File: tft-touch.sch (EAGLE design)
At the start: 2 parts

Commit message: As ordered
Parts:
- added CONN1: STEMMA_I2C_QT, 00jim:STEMMA_I2C_QT
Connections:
- new net SCL: CONN1G$1.SCL, JP1.IO22_SCL
- new net SDA: CONN1G$1.SDA, JP1.IO21_SDA
- net GND: now also CONN1G$1.GND
- net S_CS: now also JP1.IO00_XX; no longer JP1.IO22_SCL
- net T_CS: now also JP1.VP; no longer JP1.IO21_SDA
- net VCC: now also CONN1G$1.V+
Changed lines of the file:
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@@
 <part name="U$1" library="00jim" deviceset="SPI_TFT_TOUCH" device=""/>
 <part name="JP1" library="00jim" deviceset="TTGO-TS-ESP32" device=""/>
+<part name="CONN1" library="00jim" deviceset="STEMMA_I2C" device="_QT"/>
 </parts>
 <sheets>
@@
 <attribute name="NAME" x="52.07" y="76.835" size="1.778" layer="95"/>
 <attribute name="VALUE" x="52.07" y="20.32" size="1.778" layer="96"/>
+</instance>
+<instance part="CONN1" gate="G$1" x="116.84" y="66.04" smashed="yes">
+<attribute name="NAME" x="113.03" y="74.295" size="1.778" layer="95"/>
+<attribute name="VALUE" x="113.03" y="58.42" size="1.778" layer="96"/>
 </instance>
 </instances>
@@
 <label x="83.82" y="43.18" size="1.778" layer="95"/>
 </segment>
+<segment>
+<pinref part="CONN1" gate="G$1" pin="GND"/>
+<wire x1="116.84" y1="71.12" x2="106.68" y2="71.12" width="0.1524" layer="91"/>
+<label x="106.68" y="71.12" size="1.778" layer="95"/>
+</segment>
 </net>
 <net name="VCC" class="0">
@@
 <wire x1="93.98" y1="58.42" x2="83.82" y2="58.42" width="0.1524" layer="91"/>
 <label x="83.82" y="58.42" size="1.778" layer="95"/>
+</segment>
+<segment>
+<pinref part="CONN1" gate="G$1" pin="V+"/>
+<wire x1="116.84" y1="68.58" x2="106.68" y2="68.58" width="0.1524" layer="91"/>
+<label x="106.68" y="68.58" size="1.778" layer="95"/>
 </segment>
 </net>
@@
 </segment>
 <segment>
-<pinref part="JP1" gate="G$1" pin="IO21_SDA"/>
-<wire x1="55.88" y1="40.64" x2="45.72" y2="40.64" width="0.1524" layer="91"/>
-<label x="45.72" y="40.64" size="1.778" layer="95"/>
+<pinref part="JP1" gate="G$1" pin="VP"/>
+<wire x1="55.88" y1="71.12" x2="45.72" y2="71.12" width="0.1524" layer="91"/>
+<label x="45.72" y="71.12" size="1.778" layer="95"/>
 </segment>
 </net>
@@
 </segment>
 <segment>
-<pinref part="JP1" gate="G$1" pin="IO22_SCL"/>
-<wire x1="55.88" y1="35.56" x2="45.72" y2="35.56" width="0.1524" layer="91"/>
-<label x="45.72" y="35.56" size="1.778" layer="95"/>
+<pinref part="JP1" gate="G$1" pin="IO00_XX"/>
+<wire x1="55.88" y1="53.34" x2="45.72" y2="53.34" width="0.1524" layer="91"/>
+<label x="45.72" y="53.34" size="1.778" layer="95"/>
 </segment>
 </net>
@@
 </segment>
 </net>
+<net name="SDA" class="0">
+<segment>
+<pinref part="JP1" gate="G$1" pin="IO21_SDA"/>
+<wire x1="55.88" y1="40.64" x2="45.72" y2="40.64" width="0.1524" layer="91"/>
+<label x="45.72" y="40.64" size="1.778" layer="95"/>
+</segment>
+<segment>
+<pinref part="CONN1" gate="G$1" pin="SDA"/>
+<wire x1="116.84" y1="66.04" x2="106.68" y2="66.04" width="0.1524" layer="91"/>
+<label x="106.68" y="66.04" size="1.778" layer="95"/>
+</segment>
+</net>
+<net name="SCL" class="0">
+<segment>
+<pinref part="JP1" gate="G$1" pin="IO22_SCL"/>
+<wire x1="55.88" y1="35.56" x2="45.72" y2="35.56" width="0.1524" layer="91"/>
+<label x="45.72" y="35.56" size="1.778" layer="95"/>
+</segment>
+<segment>
+<pinref part="CONN1" gate="G$1" pin="SCL"/>
+<wire x1="116.84" y1="63.5" x2="106.68" y2="63.5" width="0.1524" layer="91"/>
+<label x="106.68" y="63.5" size="1.778" layer="95"/>
+</segment>
+</net>

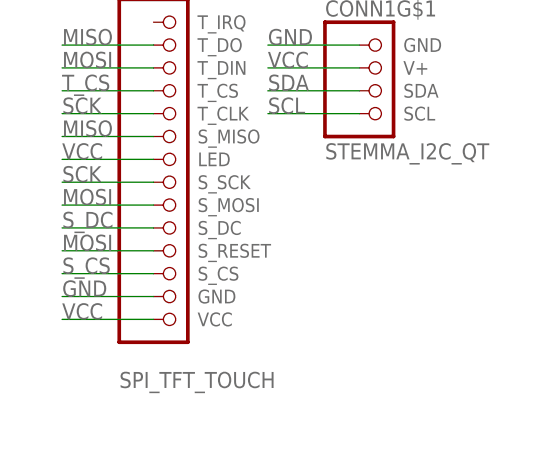
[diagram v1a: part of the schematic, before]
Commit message: Added more trinkets to TFT touch boards
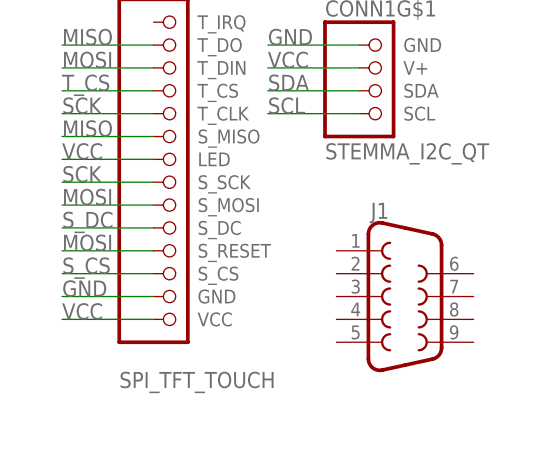
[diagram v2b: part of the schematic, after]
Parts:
- added J1: (no value), SparkFun-Connectors:DB9FEMALE
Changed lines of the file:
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@@
 <grid distance="0.1" unitdist="inch" unit="inch" style="lines" multiple="1" display="no" altdistance="0.01" altunitdist="inch" altunit="inch"/>
 <layers>
-<layer number="1" name="Top" color="4" fill="1" visible="no" active="no"/>
-<layer number="16" name="Bottom" color="1" fill="1" visible="no" active="no"/>
-<layer number="17" name="Pads" color="2" fill="1" visible="no" active="no"/>
-<layer number="18" name="Vias" color="2" fill="1" visible="no" active="no"/>
-<layer number="19" name="Unrouted" color="6" fill="1" visible="no" active="no"/>
-<layer number="20" name="Dimension" color="24" fill="1" visible="no" active="no"/>
-<layer number="21" name="tPlace" color="7" fill="1" visible="no" active="no"/>
-<layer number="22" name="bPlace" color="7" fill="1" visible="no" active="no"/>
-<layer number="23" name="tOrigins" color="15" fill="1" visible="no" active="no"/>
-<layer number="24" name="bOrigins" color="15" fill="1" visible="no" active="no"/>
-<layer number="25" name="tNames" color="7" fill="1" visible="no" active="no"/>
-<layer number="26" name="bNames" color="7" fill="1" visible="no" active="no"/>
-<layer number="27" name="tValues" color="7" fill="1" visible="no" active="no"/>
-<layer number="28" name="bValues" color="7" fill="1" visible="no" active="no"/>
+<layer number="1" name="Top" color="4" fill="1" visible="yes" active="no"/>
+<layer number="16" name="Bottom" color="1" fill="1" visible="yes" active="no"/>
+<layer number="17" name="Pads" color="2" fill="1" visible="yes" active="no"/>
+<layer number="18" name="Vias" color="2" fill="1" visible="yes" active="no"/>
+<layer number="19" name="Unrouted" color="6" fill="1" visible="yes" active="no"/>
+<layer number="20" name="Dimension" color="24" fill="1" visible="yes" active="no"/>
+<layer number="21" name="tPlace" color="7" fill="1" visible="yes" active="no"/>
+<layer number="22" name="bPlace" color="7" fill="1" visible="yes" active="no"/>
+<layer number="23" name="tOrigins" color="15" fill="1" visible="yes" active="no"/>
+<layer number="24" name="bOrigins" color="15" fill="1" visible="yes" active="no"/>
+<layer number="25" name="tNames" color="7" fill="1" visible="yes" active="no"/>
+<layer number="26" name="bNames" color="7" fill="1" visible="yes" active="no"/>
+<layer number="27" name="tValues" color="7" fill="1" visible="yes" active="no"/>
+<layer number="28" name="bValues" color="7" fill="1" visible="yes" active="no"/>
 <layer number="29" name="tStop" color="7" fill="3" visible="no" active="no"/>
 <layer number="30" name="bStop" color="7" fill="6" visible="no" active="no"/>
@@
 <layer number="35" name="tGlue" color="7" fill="4" visible="no" active="no"/>
 <layer number="36" name="bGlue" color="7" fill="5" visible="no" active="no"/>
-<layer number="37" name="tTest" color="7" fill="1" visible="no" active="no"/>
-<layer number="38" name="bTest" color="7" fill="1" visible="no" active="no"/>
+<layer number="37" name="tTest" color="7" fill="1" visible="yes" active="no"/>
+<layer number="38" name="bTest" color="7" fill="1" visible="yes" active="no"/>
 <layer number="39" name="tKeepout" color="4" fill="11" visible="no" active="no"/>
 <layer number="40" name="bKeepout" color="1" fill="11" visible="no" active="no"/>
@@
 <layer number="44" name="Drills" color="7" fill="1" visible="no" active="no"/>
 <layer number="45" name="Holes" color="7" fill="1" visible="no" active="no"/>
-<layer number="46" name="Milling" color="3" fill="1" visible="no" active="no"/>
-<layer number="47" name="Measures" color="7" fill="1" visible="no" active="no"/>
-<layer number="48" name="Document" color="7" fill="1" visible="no" active="no"/>
-<layer number="49" name="Reference" color="7" fill="1" visible="no" active="no"/>
-<layer number="50" name="dxf" color="7" fill="1" visible="no" active="no"/>
-<layer number="51" name="tDocu" color="7" fill="1" visible="no" active="no"/>
-<layer number="52" name="bDocu" color="7" fill="1" visible="no" active="no"/>
-<layer number="53" name="tGND_GNDA" color="7" fill="9" visible="no" active="no"/>
-<layer number="54" name="bGND_GNDA" color="1" fill="9" visible="no" active="no"/>
-<layer number="56" name="wert" color="7" fill="1" visible="no" active="no"/>
-<layer number="57" name="tCAD" color="7" fill="1" visible="no" active="no"/>
-<layer number="58" name="b3D" color="7" fill="1" visible="no" active="no"/>
-<layer number="59" name="tCarbon" color="7" fill="1" visible="no" active="no"/>
-<layer number="60" name="bCarbon" color="7" fill="1" visible="no" active="no"/>
-<layer number="61" name="stand" color="7" fill="1" visible="no" active="no"/>
+<layer number="46" name="Milling" color="3" fill="1" visible="yes" active="no"/>
+<layer number="47" name="Measures" color="7" fill="1" visible="yes" active="no"/>
+<layer number="48" name="Document" color="7" fill="1" visible="yes" active="no"/>
+<layer number="49" name="Reference" color="7" fill="1" visible="yes" active="no"/>
+<layer number="50" name="dxf" color="7" fill="1" visible="yes" active="no"/>
+<layer number="51" name="tDocu" color="7" fill="1" visible="yes" active="no"/>
+<layer number="52" name="bDocu" color="7" fill="1" visible="yes" active="no"/>
+<layer number="53" name="tGND_GNDA" color="7" fill="9" visible="yes" active="no"/>
+<layer number="54" name="bGND_GNDA" color="1" fill="9" visible="yes" active="no"/>
+<layer number="56" name="wert" color="7" fill="1" visible="yes" active="no"/>
+<layer number="57" name="tCAD" color="7" fill="1" visible="yes" active="no"/>
+<layer number="58" name="b3D" color="7" fill="1" visible="yes" active="no"/>
+<layer number="59" name="tCarbon" color="7" fill="1" visible="yes" active="no"/>
+<layer number="60" name="bCarbon" color="7" fill="1" visible="yes" active="no"/>
+<layer number="61" name="stand" color="7" fill="1" visible="yes" active="no"/>
 <layer number="88" name="SimResults" color="9" fill="1" visible="yes" active="yes"/>
 <layer number="89" name="SimProbes" color="9" fill="1" visible="yes" active="yes"/>
@@
 <part name="JP1" library="00jim" deviceset="TTGO-TS-ESP32" device=""/>
 <part name="CONN1" library="00jim" deviceset="STEMMA_I2C" device="_QT"/>
+<part name="J1" library="SparkFun-Connectors" deviceset="DB9" device="FEMALE"/>
 </parts>
 <sheets>
@@
 <attribute name="VALUE" x="113.03" y="58.42" size="1.778" layer="96"/>
 </instance>
+<instance part="J1" gate="G$1" x="121.92" y="43.18" smashed="yes">
+<attribute name="VALUE" x="118.11" y="34.798" size="1.778" layer="96" font="vector" align="top-left"/>
+<attribute name="NAME" x="118.11" y="51.816" size="1.778" layer="95" font="vector"/>
+</instance>
 </instances>

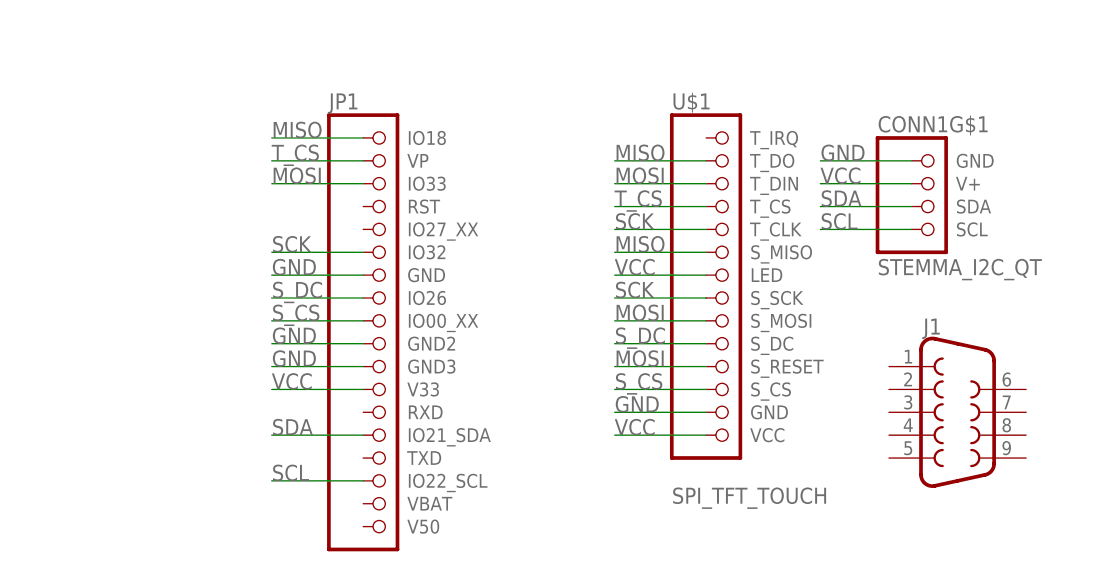
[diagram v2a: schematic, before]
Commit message: Fix board bug, order again
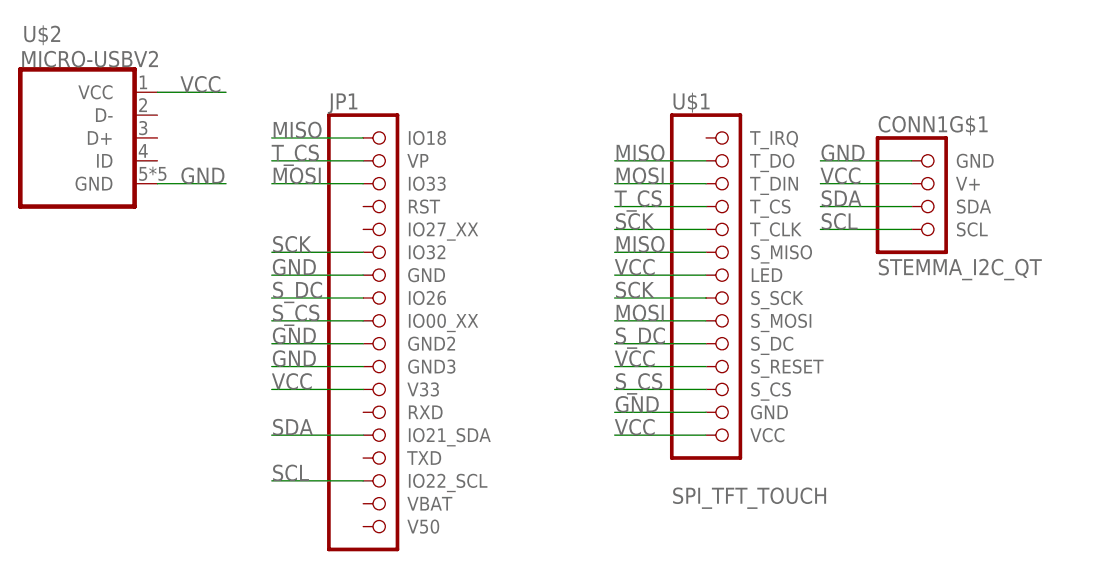
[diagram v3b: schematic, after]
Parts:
- removed J1: (no value), SparkFun-Connectors:DB9FEMALE
- added U$2: MICRO-USBV2, microusb:MICRO-USBV2
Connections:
- net GND: now also U$2.GND
- net MOSI: no longer U$1.S_RESET
- net VCC: now also U$1.S_RESET, U$2.VCC
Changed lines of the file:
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@@
 <grid distance="0.1" unitdist="inch" unit="inch" style="lines" multiple="1" display="no" altdistance="0.01" altunitdist="inch" altunit="inch"/>
 <layers>
-<layer number="1" name="Top" color="4" fill="1" visible="yes" active="no"/>
-<layer number="16" name="Bottom" color="1" fill="1" visible="yes" active="no"/>
-<layer number="17" name="Pads" color="2" fill="1" visible="yes" active="no"/>
-<layer number="18" name="Vias" color="2" fill="1" visible="yes" active="no"/>
-<layer number="19" name="Unrouted" color="6" fill="1" visible="yes" active="no"/>
-<layer number="20" name="Dimension" color="24" fill="1" visible="yes" active="no"/>
-<layer number="21" name="tPlace" color="7" fill="1" visible="yes" active="no"/>
-<layer number="22" name="bPlace" color="7" fill="1" visible="yes" active="no"/>
-<layer number="23" name="tOrigins" color="15" fill="1" visible="yes" active="no"/>
-<layer number="24" name="bOrigins" color="15" fill="1" visible="yes" active="no"/>
-<layer number="25" name="tNames" color="7" fill="1" visible="yes" active="no"/>
-<layer number="26" name="bNames" color="7" fill="1" visible="yes" active="no"/>
-<layer number="27" name="tValues" color="7" fill="1" visible="yes" active="no"/>
-<layer number="28" name="bValues" color="7" fill="1" visible="yes" active="no"/>
+<layer number="1" name="Top" color="4" fill="1" visible="no" active="no"/>
+<layer number="16" name="Bottom" color="1" fill="1" visible="no" active="no"/>
+<layer number="17" name="Pads" color="2" fill="1" visible="no" active="no"/>
+<layer number="18" name="Vias" color="2" fill="1" visible="no" active="no"/>
+<layer number="19" name="Unrouted" color="6" fill="1" visible="no" active="no"/>
+<layer number="20" name="Dimension" color="24" fill="1" visible="no" active="no"/>
+<layer number="21" name="tPlace" color="7" fill="1" visible="no" active="no"/>
+<layer number="22" name="bPlace" color="7" fill="1" visible="no" active="no"/>
+<layer number="23" name="tOrigins" color="15" fill="1" visible="no" active="no"/>
+<layer number="24" name="bOrigins" color="15" fill="1" visible="no" active="no"/>
+<layer number="25" name="tNames" color="7" fill="1" visible="no" active="no"/>
+<layer number="26" name="bNames" color="7" fill="1" visible="no" active="no"/>
+<layer number="27" name="tValues" color="7" fill="1" visible="no" active="no"/>
+<layer number="28" name="bValues" color="7" fill="1" visible="no" active="no"/>
 <layer number="29" name="tStop" color="7" fill="3" visible="no" active="no"/>
 <layer number="30" name="bStop" color="7" fill="6" visible="no" active="no"/>
@@
 <layer number="35" name="tGlue" color="7" fill="4" visible="no" active="no"/>
 <layer number="36" name="bGlue" color="7" fill="5" visible="no" active="no"/>
-<layer number="37" name="tTest" color="7" fill="1" visible="yes" active="no"/>
-<layer number="38" name="bTest" color="7" fill="1" visible="yes" active="no"/>
+<layer number="37" name="tTest" color="7" fill="1" visible="no" active="no"/>
+<layer number="38" name="bTest" color="7" fill="1" visible="no" active="no"/>
 <layer number="39" name="tKeepout" color="4" fill="11" visible="no" active="no"/>
 <layer number="40" name="bKeepout" color="1" fill="11" visible="no" active="no"/>
@@
 <layer number="44" name="Drills" color="7" fill="1" visible="no" active="no"/>
 <layer number="45" name="Holes" color="7" fill="1" visible="no" active="no"/>
-<layer number="46" name="Milling" color="3" fill="1" visible="yes" active="no"/>
-<layer number="47" name="Measures" color="7" fill="1" visible="yes" active="no"/>
-<layer number="48" name="Document" color="7" fill="1" visible="yes" active="no"/>
-<layer number="49" name="Reference" color="7" fill="1" visible="yes" active="no"/>
-<layer number="50" name="dxf" color="7" fill="1" visible="yes" active="no"/>
-<layer number="51" name="tDocu" color="7" fill="1" visible="yes" active="no"/>
-<layer number="52" name="bDocu" color="7" fill="1" visible="yes" active="no"/>
-<layer number="53" name="tGND_GNDA" color="7" fill="9" visible="yes" active="no"/>
-<layer number="54" name="bGND_GNDA" color="1" fill="9" visible="yes" active="no"/>
-<layer number="56" name="wert" color="7" fill="1" visible="yes" active="no"/>
-<layer number="57" name="tCAD" color="7" fill="1" visible="yes" active="no"/>
-<layer number="58" name="b3D" color="7" fill="1" visible="yes" active="no"/>
-<layer number="59" name="tCarbon" color="7" fill="1" visible="yes" active="no"/>
-<layer number="60" name="bCarbon" color="7" fill="1" visible="yes" active="no"/>
-<layer number="61" name="stand" color="7" fill="1" visible="yes" active="no"/>
+<layer number="46" name="Milling" color="3" fill="1" visible="no" active="no"/>
+<layer number="47" name="Measures" color="7" fill="1" visible="no" active="no"/>
+<layer number="48" name="Document" color="7" fill="1" visible="no" active="no"/>
+<layer number="49" name="Reference" color="7" fill="1" visible="no" active="no"/>
+<layer number="50" name="dxf" color="7" fill="1" visible="no" active="no"/>
+<layer number="51" name="tDocu" color="7" fill="1" visible="no" active="no"/>
+<layer number="52" name="bDocu" color="7" fill="1" visible="no" active="no"/>
+<layer number="53" name="tGND_GNDA" color="7" fill="9" visible="no" active="no"/>
+<layer number="54" name="bGND_GNDA" color="1" fill="9" visible="no" active="no"/>
+<layer number="56" name="wert" color="7" fill="1" visible="no" active="no"/>
+<layer number="57" name="tCAD" color="7" fill="1" visible="no" active="no"/>
+<layer number="58" name="b3D" color="7" fill="1" visible="no" active="no"/>
+<layer number="59" name="tCarbon" color="7" fill="1" visible="no" active="no"/>
+<layer number="60" name="bCarbon" color="7" fill="1" visible="no" active="no"/>
+<layer number="61" name="stand" color="7" fill="1" visible="no" active="no"/>
 <layer number="88" name="SimResults" color="9" fill="1" visible="yes" active="yes"/>
 <layer number="89" name="SimProbes" color="9" fill="1" visible="yes" active="yes"/>
@@
 <part name="JP1" library="00jim" deviceset="TTGO-TS-ESP32" device=""/>
 <part name="CONN1" library="00jim" deviceset="STEMMA_I2C" device="_QT"/>
-<part name="J1" library="SparkFun-Connectors" deviceset="DB9" device="FEMALE"/>
+<part name="U$2" library="microusb" deviceset="MICRO-USB" device="V2"/>
 </parts>
 <sheets>
@@
 <attribute name="VALUE" x="113.03" y="58.42" size="1.778" layer="96"/>
 </instance>
-<instance part="J1" gate="G$1" x="121.92" y="43.18" smashed="yes">
-<attribute name="VALUE" x="118.11" y="34.798" size="1.778" layer="96" font="vector" align="top-left"/>
-<attribute name="NAME" x="118.11" y="51.816" size="1.778" layer="95" font="vector"/>
+<instance part="U$2" gate="G$1" x="17.78" y="81.28" smashed="yes">
+<attribute name="NAME" x="18.034" y="84.328" size="1.778" layer="95"/>
+<attribute name="VALUE" x="17.78" y="81.534" size="1.778" layer="96"/>
 </instance>
 </instances>
@@
 <label x="106.68" y="71.12" size="1.778" layer="95"/>
 </segment>
+<segment>
+<pinref part="U$2" gate="G$1" pin="GND"/>
+<wire x1="33.02" y1="68.58" x2="40.64" y2="68.58" width="0.1524" layer="91"/>
+<label x="35.56" y="68.58" size="1.778" layer="95"/>
+</segment>
 </net>
 <net name="VCC" class="0">
@@
 <label x="106.68" y="68.58" size="1.778" layer="95"/>
 </segment>
+<segment>
+<pinref part="U$1" gate="G$1" pin="S_RESET"/>
+<wire x1="93.98" y1="48.26" x2="83.82" y2="48.26" width="0.1524" layer="91"/>
+<label x="83.82" y="48.26" size="1.778" layer="95"/>
+</segment>
+<segment>
+<pinref part="U$2" gate="G$1" pin="VCC"/>
+<wire x1="33.02" y1="78.74" x2="40.64" y2="78.74" width="0.1524" layer="91"/>
+<label x="35.56" y="78.74" size="1.778" layer="95"/>
+</segment>
 </net>
 <net name="MISO" class="0">
@@
 <net name="MOSI" class="0">
 <segment>
-<pinref part="U$1" gate="G$1" pin="S_RESET"/>
-<wire x1="93.98" y1="48.26" x2="83.82" y2="48.26" width="0.1524" layer="91"/>
-<label x="83.82" y="48.26" size="1.778" layer="95"/>
-</segment>
-<segment>
 <pinref part="U$1" gate="G$1" pin="S_MOSI"/>
